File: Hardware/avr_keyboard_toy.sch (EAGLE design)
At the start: 22 parts, among them IC1 7805T, IC2 MCP23017SP, U1 ATMEGA328P-PU

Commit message: Working on Rev B of hardware
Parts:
- removed C1, C2: 10uF, adafruit:CPOL-USE1.8-4
- removed IC1: 7805T, adafruit:7805T
- IC2: value MCP23017SP -> MCP23017SO; device adafruit:MCP23017SP -> adafruit:MCP23017SO
- U1: value ATMEGA328P-PU -> ATMEGA328P-AU; device Atmel_By_element14_Batch_1-00:ATMEGA328P-PU -> Atmel_By_element14_Batch_1-00:ATMEGA328P-AU
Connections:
- new net ADC6: U1.ADC6
- new net ADC7: U1.ADC7
- net +3V3: no longer C2.+, IC1.VO
- net +5V: no longer C1.+, IC1.VI
- net GND: now also U1.GND_3; no longer C1.-, C2.-, IC1.GND
- net VCC: now also U1.VCC_2
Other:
- moved on the sheet: R3, XTAL1

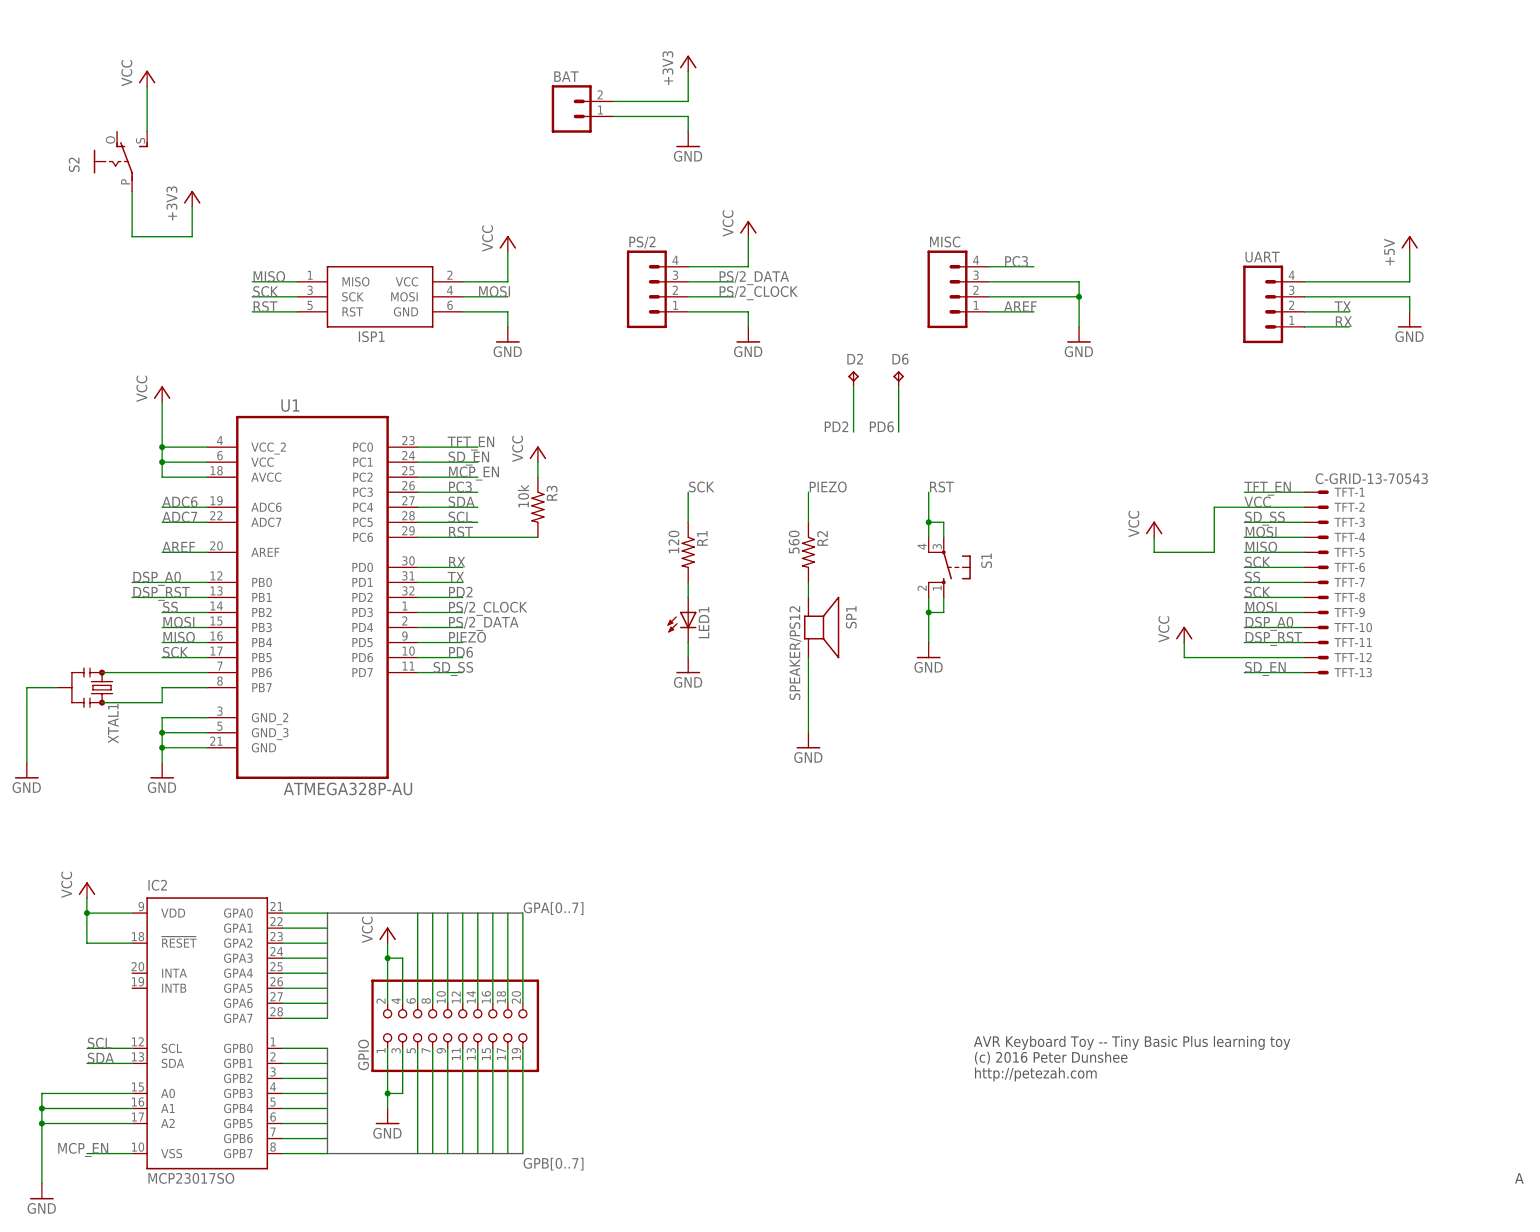
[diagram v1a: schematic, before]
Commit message: Added SID test, and made rev B of board
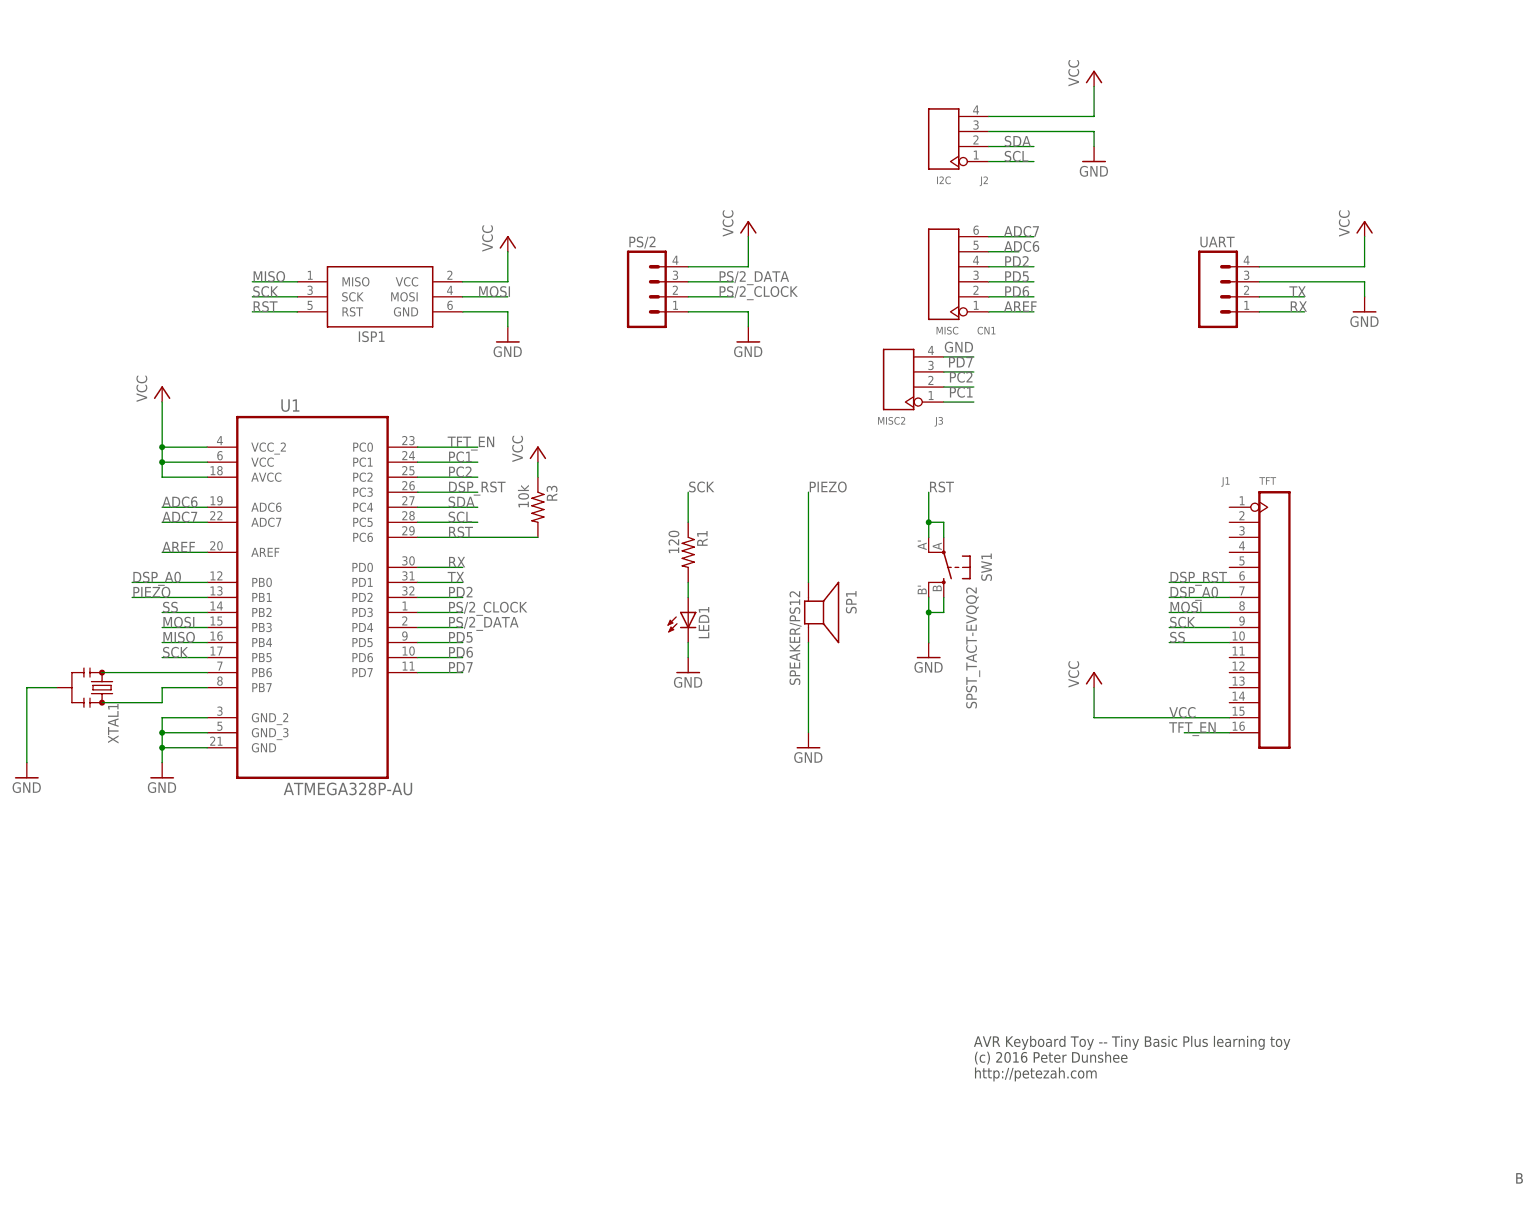
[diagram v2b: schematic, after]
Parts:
- removed BAT: (no value), SparkFun-Connectors:M02PTH
- removed D2, D6: TPB1,27, testpad:TPB1,27
- removed GPIO: (no value), SparkFun-Connectors:PINHD-2X10
- removed IC2: MCP23017SO, adafruit:MCP23017SO
- removed MISC: (no value), SparkFun-Connectors:M04PTH
- removed R2: 560, adafruit:R-US_0204/5
- removed S1: (no value), switch-omron:10-XX
- removed S2: (no value), adafruit:EG1218S
- removed TFT: C-GRID-13-70543, con-molex:C-GRID-13-70543
- added CN1: MISC, Seeed-Connector -2016:DIP-BLACK-FEMALE-HEADER-VERT(6P-2.54)
- added J1: TFT, Seeed-OPL-Connector:DIP-BLACK-FEMALE-HEADER-VERT(16P-2.54)
- added J2: I2C, Seeed-Connector -2016:DIP-BLACK-FEMALE-HEADER-VERT(4P-2.54)
- added J3: MISC2, Seeed-Connector -2016:DIP-BLACK-FEMALE-HEADER-VERT(4P-2.54)
- added SW1: SPST_TACT-EVQQ2, adafruit:SPST_TACT-EVQQ2
- LED1: device adafruit:LED3MM -> adafruit:LEDCHIPLED_1206
- R1, R3: device adafruit:R-US_0204/5 -> adafruit:R-US_R1206
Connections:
- removed net +3V3: BAT.2, S2.P
- removed net +5V: UART.4
- removed net GPA0: GPIO.6, IC2.GPA0
- removed net GPA1: GPIO.8, IC2.GPA1
- removed net GPA2: GPIO.10, IC2.GPA2
- removed net GPA3: GPIO.12, IC2.GPA3
- removed net GPA4: GPIO.14, IC2.GPA4
- removed net GPA5: GPIO.16, IC2.GPA5
- removed net GPA6: GPIO.18, IC2.GPA6
- removed net GPA7: GPIO.20, IC2.GPA7
- removed net GPB0: GPIO.5, IC2.GPB0
- removed net GPB1: GPIO.7, IC2.GPB1
- removed net GPB2: GPIO.9, IC2.GPB2
- removed net GPB3: GPIO.11, IC2.GPB3
- removed net GPB4: GPIO.13, IC2.GPB4
- removed net GPB5: GPIO.15, IC2.GPB5
- removed net GPB6: GPIO.17, IC2.GPB6
- removed net GPB7: GPIO.19, IC2.GPB7
- removed net MCP_EN: IC2.VSS, U1.PC2
- removed net N$4: R2.2, SP1.+
- removed net PC3: MISC.4, U1.PC3
- removed net SD_EN: TFT-13.S, U1.PC1
- removed net SD_SS: TFT-3.S, U1.PD7
- new net PC1: J3.P$1, U1.PC1
- new net PC2: J3.P$2, U1.PC2
- new net PD5: CN1.3, U1.PD5
- new net PD7: J3.P$3, U1.PD7
- net ADC6: now also CN1.5
- net ADC7: now also CN1.6
- net AREF: now also CN1.1; no longer MISC.1
- net DSP_A0: now also J1.7; no longer TFT-10.S
- net DSP_RST: now also J1.6, U1.PC3; no longer TFT-11.S, U1.PB1
- net GND: now also J2.P$3, J3.P$4, SW1.S, SW1.S1; no longer BAT.1, GPIO.1, GPIO.3, IC2.A0, IC2.A1, IC2.A2, MISC.2, MISC.3, S1.S, S1.S1
- net MISO: no longer TFT-5.S
- net MOSI: now also J1.8; no longer TFT-4.S, TFT-9.S
- net PD2: now also CN1.4; no longer D2.TP
- net PD6: now also CN1.2; no longer D6.TP
- net PIEZO: now also SP1.+, U1.PB1; no longer R2.1, U1.PD5
- net RST: now also SW1.P, SW1.P1; no longer S1.P, S1.P1
- net SCK: now also J1.9; no longer TFT-6.S, TFT-8.S
- net SCL: now also J2.P$1; no longer IC2.SCL
- net SDA: now also J2.P$2; no longer IC2.SDA
- net SS: now also J1.10; no longer TFT-7.S
- net TFT_EN: now also J1.16; no longer TFT-1.S
- net VCC: now also J1.15, J2.P$4, UART.4; no longer GPIO.2, GPIO.4, IC2.!RESET, IC2.VDD, S2.S, TFT-12.S, TFT-2.S
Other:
- note added: "B"
- note removed: "A"
- moved on the sheet: SP1, UART

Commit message: Made the board a bit more configurable Added jumpers to allow me to configure one board for one display board, and another one for a different one.
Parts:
- added BL_JP, GND_JP: (no value), jumper:SJ
- added SS_VCC_JP: (no value), jumper:SJ2W
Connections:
- new net BL_JP: BL_JP.2, J1.11
- new net GND_JP: GND_JP.2, J1.12
- new net SS_VCC_JP: J1.10, SS_VCC_JP.2
- net PD2: now also J1.5
- net SS: now also SS_VCC_JP.3; no longer J1.10
- net TFT_EN: now also GND_JP.1
- net VCC: now also BL_JP.1, SS_VCC_JP.1
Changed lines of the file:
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@@
 <part name="CN1" library="Seeed-Connector -2016" deviceset="DIP-BLACK-FEMALE-HEADER-VERT(6P-2.54)" device="" value="MISC"/>
 <part name="J3" library="Seeed-Connector -2016" deviceset="DIP-BLACK-FEMALE-HEADER-VERT(4P-2.54)" device="" value="MISC2"/>
+<part name="SS_VCC_JP" library="jumper" deviceset="SJ2W" device=""/>
+<part name="BL_JP" library="jumper" deviceset="SJ" device=""/>
+<part name="GND_JP" library="jumper" deviceset="SJ" device=""/>
 </parts>
 <sheets>
@@
 <instance part="CN1" gate="G$1" x="152.4" y="151.13" rot="R180"/>
 <instance part="J3" gate="G$1" x="144.78" y="133.35" rot="R180"/>
+<instance part="SS_VCC_JP" gate="G$1" x="182.88" y="88.9" rot="R180"/>
+<instance part="BL_JP" gate="1" x="134.62" y="43.18"/>
+<instance part="GND_JP" gate="1" x="167.64" y="43.18"/>
 </instances>
 <busses>
@@
 </segment>
 <segment>
-<wire x1="190.5" y1="88.9" x2="200.66" y2="88.9" width="0.1524" layer="91"/>
-<label x="190.5" y="88.9" size="1.778" layer="95"/>
-<pinref part="J1" gate="G$1" pin="10"/>
+<pinref part="SS_VCC_JP" gate="G$1" pin="3"/>
+<wire x1="182.88" y1="99.06" x2="182.88" y2="93.98" width="0.1524" layer="91"/>
+<label x="180.34" y="96.52" size="1.778" layer="95"/>
 </segment>
 </net>
@@
 <segment>
 <pinref part="J1" gate="G$1" pin="15"/>
-<wire x1="177.8" y1="76.2" x2="200.66" y2="76.2" width="0.1524" layer="91"/>
+<wire x1="177.8" y1="76.2" x2="182.88" y2="76.2" width="0.1524" layer="91"/>
 <label x="190.5" y="76.2" size="1.778" layer="95"/>
+<pinref part="SS_VCC_JP" gate="G$1" pin="1"/>
+<wire x1="182.88" y1="76.2" x2="200.66" y2="76.2" width="0.1524" layer="91"/>
+<wire x1="182.88" y1="83.82" x2="182.88" y2="76.2" width="0.1524" layer="91"/>
+<junction x="182.88" y="76.2"/>
 </segment>
 <segment>
@@
 <pinref part="J2" gate="G$1" pin="P$4"/>
 </segment>
+<segment>
+<pinref part="BL_JP" gate="1" pin="1"/>
+<wire x1="121.92" y1="43.18" x2="129.54" y2="43.18" width="0.1524" layer="91"/>
+<label x="121.92" y="43.18" size="1.778" layer="95"/>
+</segment>
 </net>
 <net name="PS/2_DATA" class="0">
@@
 <label x="190.5" y="73.66" size="1.778" layer="95"/>
 </segment>
+<segment>
+<pinref part="GND_JP" gate="1" pin="1"/>
+<wire x1="152.4" y1="43.18" x2="162.56" y2="43.18" width="0.1524" layer="91"/>
+<label x="152.4" y="43.18" size="1.778" layer="95"/>
+</segment>
 </net>
 <net name="AREF" class="0">
@@
 <pinref part="CN1" gate="G$1" pin="4"/>
 </segment>
+<segment>
+<pinref part="J1" gate="G$1" pin="5"/>
+<wire x1="190.5" y1="101.6" x2="200.66" y2="101.6" width="0.1524" layer="91"/>
+<label x="190.5" y="101.6" size="1.778" layer="95"/>
+</segment>
 </net>
 <net name="PD6" class="0">
@@
 </segment>
 </net>
+<net name="SS_VCC_JP" class="0">
+<segment>
+<wire x1="187.96" y1="88.9" x2="200.66" y2="88.9" width="0.1524" layer="91"/>
+<label x="185.42" y="88.9" size="1.778" layer="95"/>
+<pinref part="J1" gate="G$1" pin="10"/>
+<pinref part="SS_VCC_JP" gate="G$1" pin="2"/>
+</segment>
+</net>
+<net name="BL_JP" class="0">
+<segment>
+<pinref part="J1" gate="G$1" pin="11"/>
+<wire x1="190.5" y1="86.36" x2="200.66" y2="86.36" width="0.1524" layer="91"/>
+<label x="190.5" y="86.36" size="1.778" layer="95"/>
+</segment>
+<segment>
+<pinref part="BL_JP" gate="1" pin="2"/>
+<wire x1="147.32" y1="43.18" x2="139.7" y2="43.18" width="0.1524" layer="91"/>
+<label x="142.24" y="43.18" size="1.778" layer="95"/>
+</segment>
+</net>
+<net name="GND_JP" class="0">
+<segment>
+<pinref part="J1" gate="G$1" pin="12"/>
+<wire x1="190.5" y1="83.82" x2="200.66" y2="83.82" width="0.1524" layer="91"/>
+<label x="190.5" y="83.82" size="1.778" layer="95"/>
+</segment>
+<segment>
+<pinref part="GND_JP" gate="1" pin="2"/>
+<wire x1="182.88" y1="43.18" x2="172.72" y2="43.18" width="0.1524" layer="91"/>
+<label x="175.26" y="43.18" size="1.778" layer="95"/>
+</segment>
+</net>
